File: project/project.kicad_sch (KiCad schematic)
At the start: 4 parts, among them J1 flasher, U1 ESP32-WROOM-32

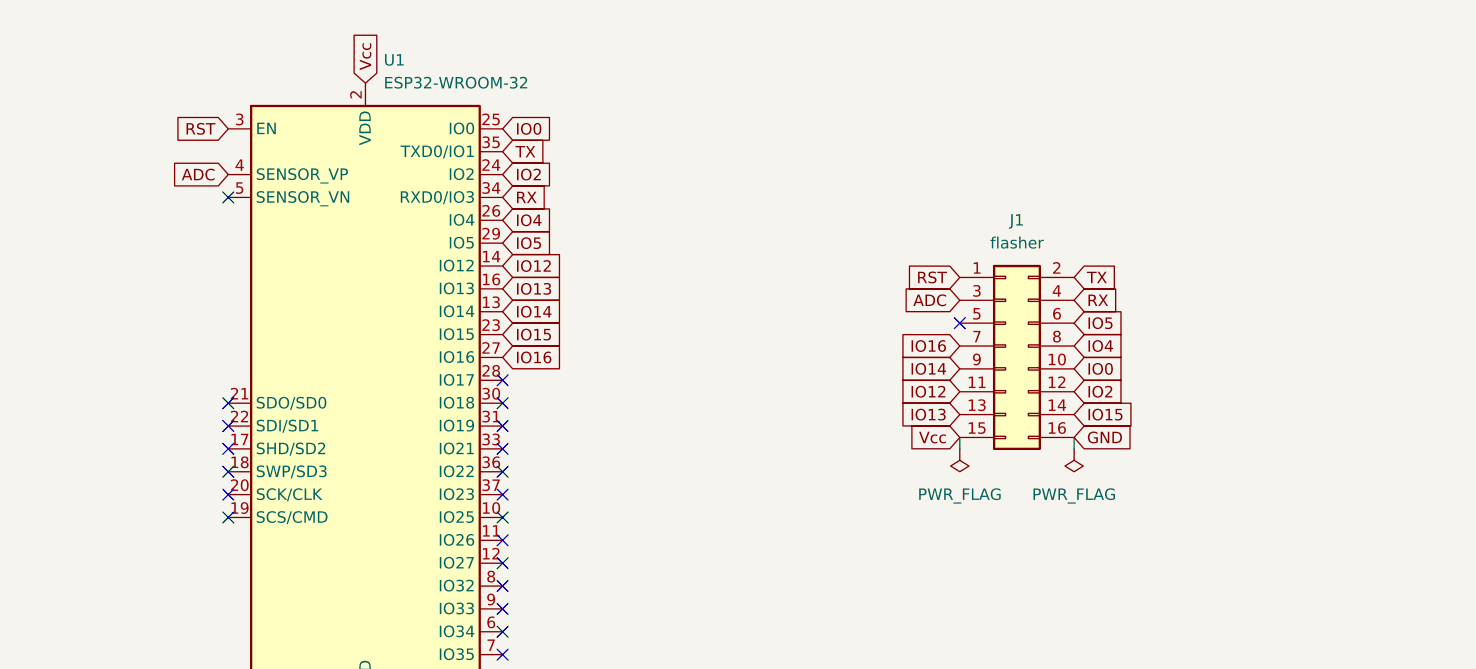
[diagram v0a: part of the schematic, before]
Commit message: using smaller 2x4 connector and shrinking pcb
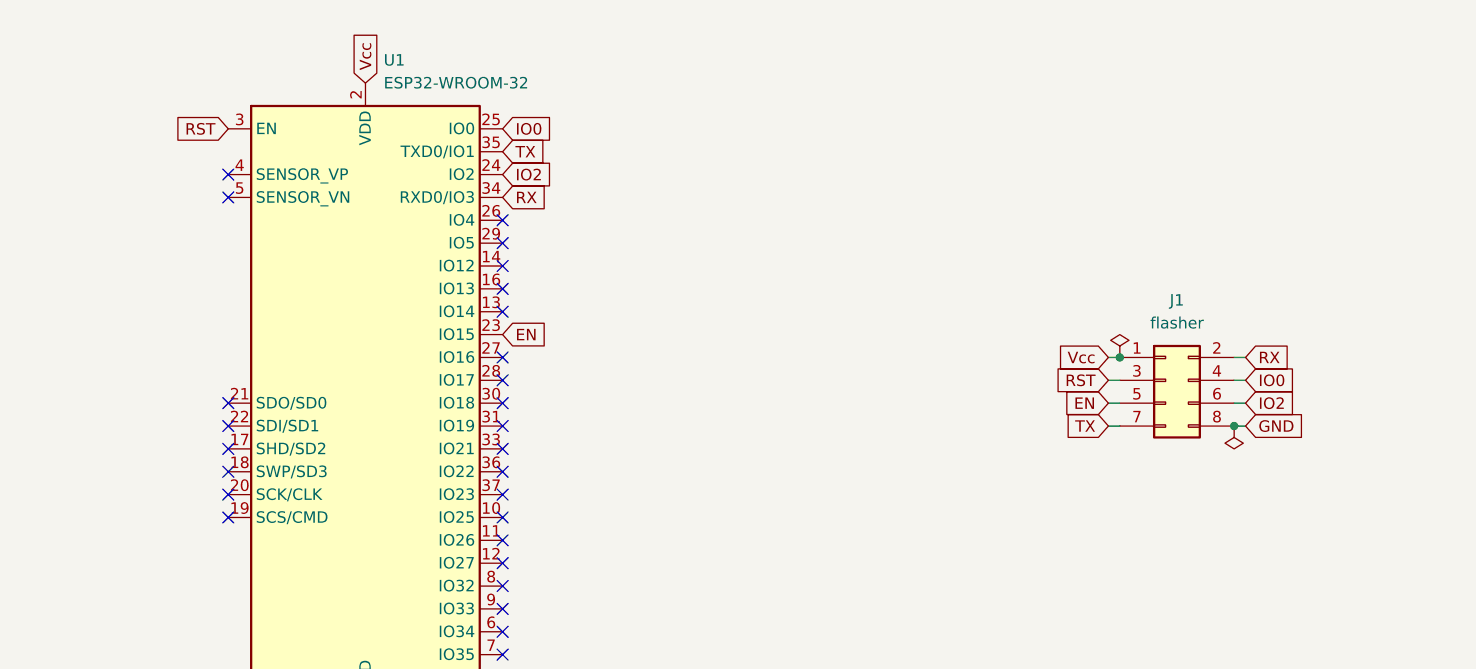
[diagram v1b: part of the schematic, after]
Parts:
- removed J1: flasher, Connector_IDC:IDC-Header_2x08_P2.54mm_Vertical, symbol Connector_Generic:Conn_02x08_Odd_Even
- added J1: flasher, Connector_IDC:IDC-Header_2x04_P2.54mm_Vertical, symbol Connector_Generic:Conn_02x04_Odd_Even
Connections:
- net GND: now also J1.8 (Pin_8)
- net IO0: now also J1.4 (Pin_4)
- net IO2: now also J1.6 (Pin_6)
- net RST: now also J1.3 (Pin_3)
- net RX: now also J1.2 (Pin_2)
- net TX: now also J1.7 (Pin_7)
- net Vcc: now also J1.1 (Pin_1)
- net ADC: no longer names the net of U1.4 (SENSOR_VP)
- net IO12: no longer names the net of U1.14 (IO12)
- net IO13: no longer names the net of U1.16 (IO13)
- net IO14: no longer names the net of U1.13 (IO14)
- net IO15 renamed EN
- net EN: now also J1.5 (Pin_5)
- net IO16: no longer names the net of U1.27 (IO16)
- net IO4: no longer names the net of U1.26 (IO4)
- net IO5: no longer names the net of U1.29 (IO5)
- no-connect marks 21 -> 27

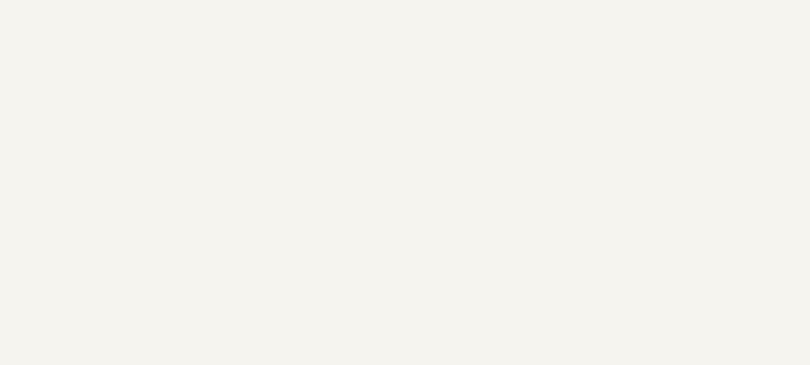
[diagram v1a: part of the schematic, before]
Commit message: adding 4 screwholes for mounting
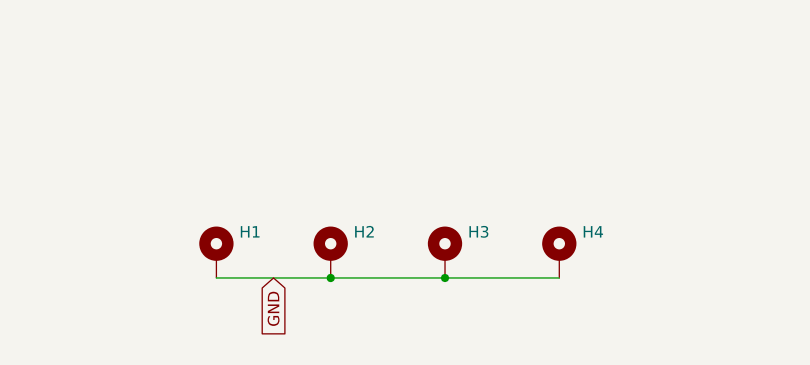
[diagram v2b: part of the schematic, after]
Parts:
- added H1, H2, H3, H4: MountingHole_Pad, -local:MountingHole_1.35mm_M1.2_Pad, symbol Mechanical:MountingHole_Pad
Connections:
- net GND: now also H1.1, H2.1, H3.1, H4.1
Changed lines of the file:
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@@
   (title_block
     (title "esp-flasher-32")
-    (date "2023-08-18")
-    (rev "2.1")
     (company "makerspace.lt")
   )
   (junction (at 184.15 83.82) (diameter 0) (color 0 0 0 0)
   )
+  (junction (at 152.4 177.8) (diameter 0) (color 0 0 0 0)
+  )
   (junction (at 196.85 91.44) (diameter 0) (color 0 0 0 0)
+  )
+  (junction (at 139.7 177.8) (diameter 0) (color 0 0 0 0)
   )
   (no_connect (at 115.57 93.98))
@@
     (stroke (width 0) (type default) (color 0 0 0 0))
   )
+  (wire (pts (xy 152.4 177.8) (xy 165.1 177.8))
+    (stroke (width 0) (type default) (color 0 0 0 0))
+  )
   (wire (pts (xy 198.12 91.44) (xy 196.85 91.44))
     (stroke (width 0) (type default) (color 0 0 0 0))
@@
     (stroke (width 0) (type default) (color 0 0 0 0))
   )
+  (wire (pts (xy 139.7 177.8) (xy 152.4 177.8))
+    (stroke (width 0) (type default) (color 0 0 0 0))
+  )
+  (wire (pts (xy 127 177.8) (xy 139.7 177.8))
+    (stroke (width 0) (type default) (color 0 0 0 0))
+  )
   (global_label "IO2" (shape input) (at 198.12 88.9 0) (fields_autoplaced)
     (effects (font (size 1.27 1.27)) (justify left))
@@
     (effects (font (size 1.27 1.27)) (justify right))
     (property "Intersheet References" "${INTERSHEET_REFS}" (id 0) (at 178.2898 91.5194 0)
+      (effects (font (size 1.27 1.27)) (justify right) hide)
+    )
+  )
+  (global_label "GND" (shape input) (at 133.35 177.8 270) (fields_autoplaced)
+    (effects (font (size 1.27 1.27)) (justify right))
+    (property "Intersheet References" "${INTERSHEET_REFS}" (id 0) (at 133.2706 184.0836 90)
       (effects (font (size 1.27 1.27)) (justify right) hide)
     )
@@
     (pin "8")
   )
+  (symbol (lib_id "Mechanical:MountingHole_Pad") (at 127 175.26 0) (unit 1)
+    (in_bom yes) (on_board yes) (fields_autoplaced)
+    (property "Reference" "H1" (id 0) (at 129.54 172.7199 0)
+      (effects (font (size 1.27 1.27)) (justify left))
+    )
+    (property "Value" "MountingHole_Pad" (id 1) (at 129.54 175.2599 0)
+      (effects (font (size 1.27 1.27)) (justify left) hide)
+    )
+    (property "Footprint" "-local:MountingHole_1.35mm_M1.2_Pad" (id 2) (at 127 175.26 0)
+      (effects (font (size 1.27 1.27)) hide)
+    )
+    (property "Datasheet" "~" (id 3) (at 127 175.26 0)
+      (effects (font (size 1.27 1.27)) hide)
+    )
+    (pin "1")
+  )
+  (symbol (lib_id "Mechanical:MountingHole_Pad") (at 165.1 175.26 0) (unit 1)
+    (in_bom yes) (on_board yes) (fields_autoplaced)
+    (property "Reference" "H4" (id 0) (at 167.64 172.7199 0)
+      (effects (font (size 1.27 1.27)) (justify left))
+    )
+    (property "Value" "MountingHole_Pad" (id 1) (at 167.64 175.2599 0)
+      (effects (font (size 1.27 1.27)) (justify left) hide)
+    )
+    (property "Footprint" "-local:MountingHole_1.35mm_M1.2_Pad" (id 2) (at 165.1 175.26 0)
+      (effects (font (size 1.27 1.27)) hide)
+    )
+    (property "Datasheet" "~" (id 3) (at 165.1 175.26 0)
+      (effects (font (size 1.27 1.27)) hide)
+    )
+    (pin "1")
+  )
+  (symbol (lib_id "Mechanical:MountingHole_Pad") (at 152.4 175.26 0) (unit 1)
+    (in_bom yes) (on_board yes) (fields_autoplaced)
+    (property "Reference" "H3" (id 0) (at 154.94 172.7199 0)
+      (effects (font (size 1.27 1.27)) (justify left))
+    )
+    (property "Value" "MountingHole_Pad" (id 1) (at 154.94 175.2599 0)
+      (effects (font (size 1.27 1.27)) (justify left) hide)
+    )
+    (property "Footprint" "-local:MountingHole_1.35mm_M1.2_Pad" (id 2) (at 152.4 175.26 0)
+      (effects (font (size 1.27 1.27)) hide)
+    )
+    (property "Datasheet" "~" (id 3) (at 152.4 175.26 0)
+      (effects (font (size 1.27 1.27)) hide)
+    )
+    (pin "1")
+  )
   (symbol (lib_id "power:PWR_FLAG") (at 184.15 83.82 0) (unit 1)
     (in_bom yes) (on_board yes) (fields_autoplaced)
@@
     )
     (property "Datasheet" "~" (id 3) (at 184.15 83.82 0)
+      (effects (font (size 1.27 1.27)) hide)
+    )
+    (pin "1")
+  )
+  (symbol (lib_id "Mechanical:MountingHole_Pad") (at 139.7 175.26 0) (unit 1)
+    (in_bom yes) (on_board yes) (fields_autoplaced)
+    (property "Reference" "H2" (id 0) (at 142.24 172.7199 0)
+      (effects (font (size 1.27 1.27)) (justify left))
+    )
+    (property "Value" "MountingHole_Pad" (id 1) (at 142.24 175.2599 0)
+      (effects (font (size 1.27 1.27)) (justify left) hide)
+    )
+    (property "Footprint" "-local:MountingHole_1.35mm_M1.2_Pad" (id 2) (at 139.7 175.26 0)
+      (effects (font (size 1.27 1.27)) hide)
+    )
+    (property "Datasheet" "~" (id 3) (at 139.7 175.26 0)
       (effects (font (size 1.27 1.27)) hide)
     )
@@
       (reference "G2") (unit 1) (value "LOGO_KMS") (footprint "-local:logo_kms_small_silkscreen")
     )
+    (path "/62316d7f-2776-43b9-a5e7-49fa1178d68c"
+      (reference "H1") (unit 1) (value "MountingHole_Pad") (footprint "-local:MountingHole_1.35mm_M1.2_Pad")
+    )
+    (path "/a7eb0e72-e2f1-4ad6-bd98-9a48fc46d3d7"
+      (reference "H2") (unit 1) (value "MountingHole_Pad") (footprint "-local:MountingHole_1.35mm_M1.2_Pad")
+    )
+    (path "/8603ffe2-cbbc-4cf4-8c13-48eb0b2590ca"
+      (reference "H3") (unit 1) (value "MountingHole_Pad") (footprint "-local:MountingHole_1.35mm_M1.2_Pad")
+    )
+    (path "/825f36ef-f6b1-4a01-b92c-344d5a0eb786"
+      (reference "H4") (unit 1) (value "MountingHole_Pad") (footprint "-local:MountingHole_1.35mm_M1.2_Pad")
+    )
     (path "/3c51f8d5-446e-4081-bf85-8897f8b9fa5b"
